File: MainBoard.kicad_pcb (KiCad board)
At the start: 4 copper layers, 102 parts, among them J1 USB B Mini, J5 Audio Out Port, P1 CARTRIDGE_SLOT, P2 FRONT_PANEL_CONNECTOR, P4 Multi AV Out, Q1 2SC4699, SW1 RESET, U1 S-CPU, U11 PST529D, U13 S-SMP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

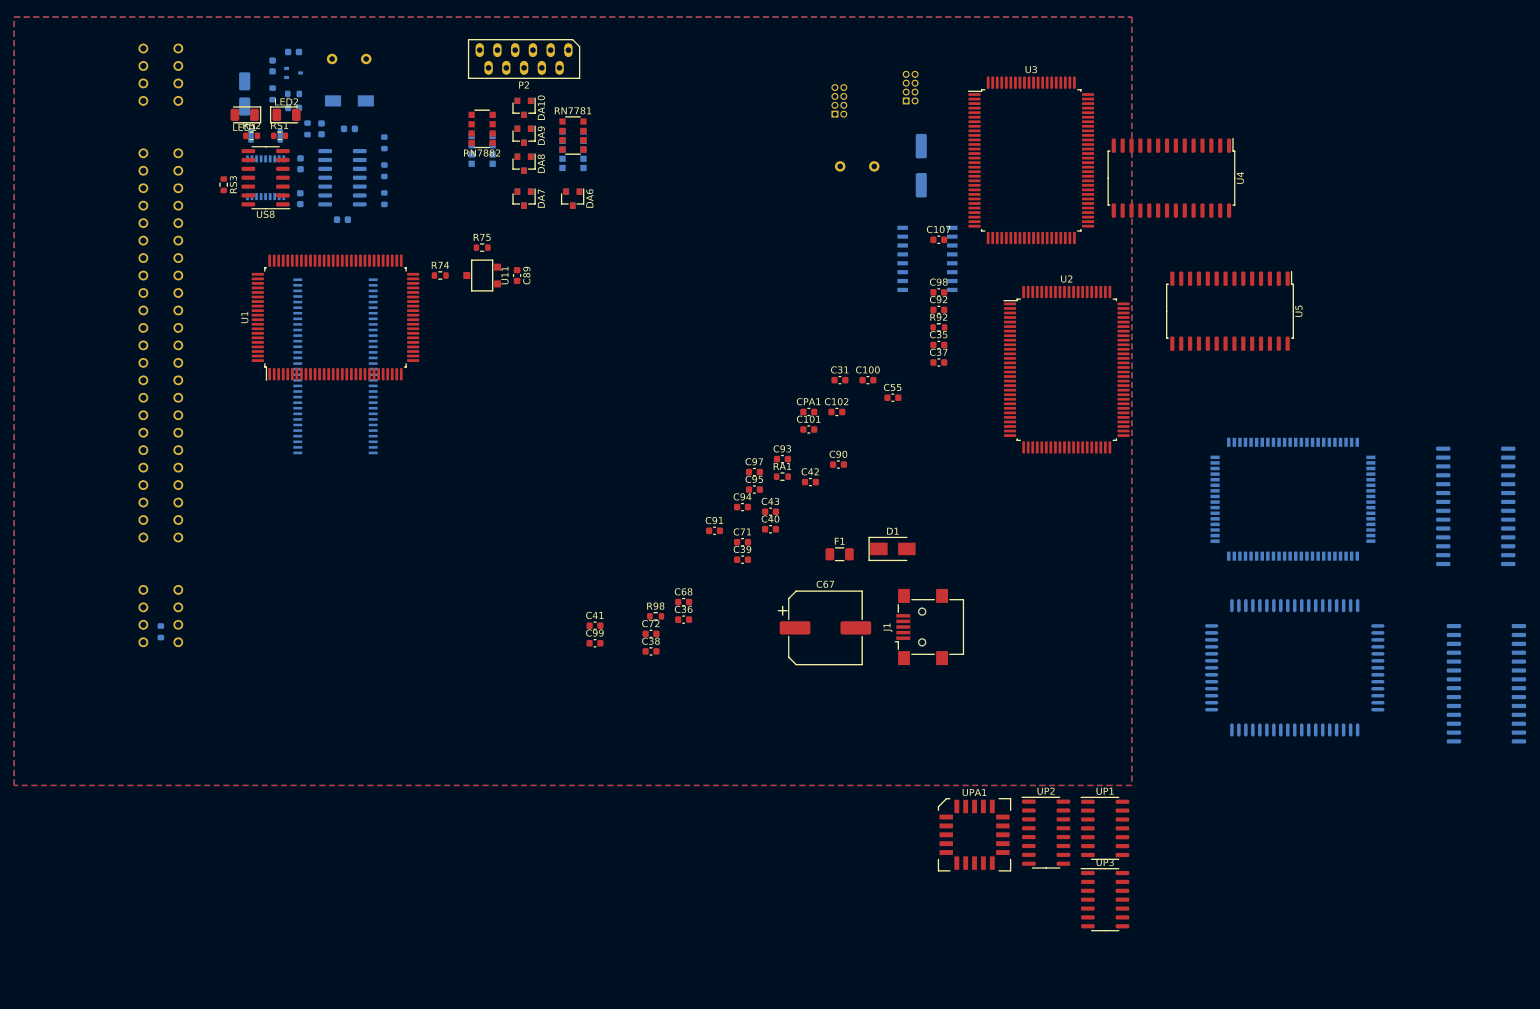
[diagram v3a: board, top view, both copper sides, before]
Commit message: Component layout is done
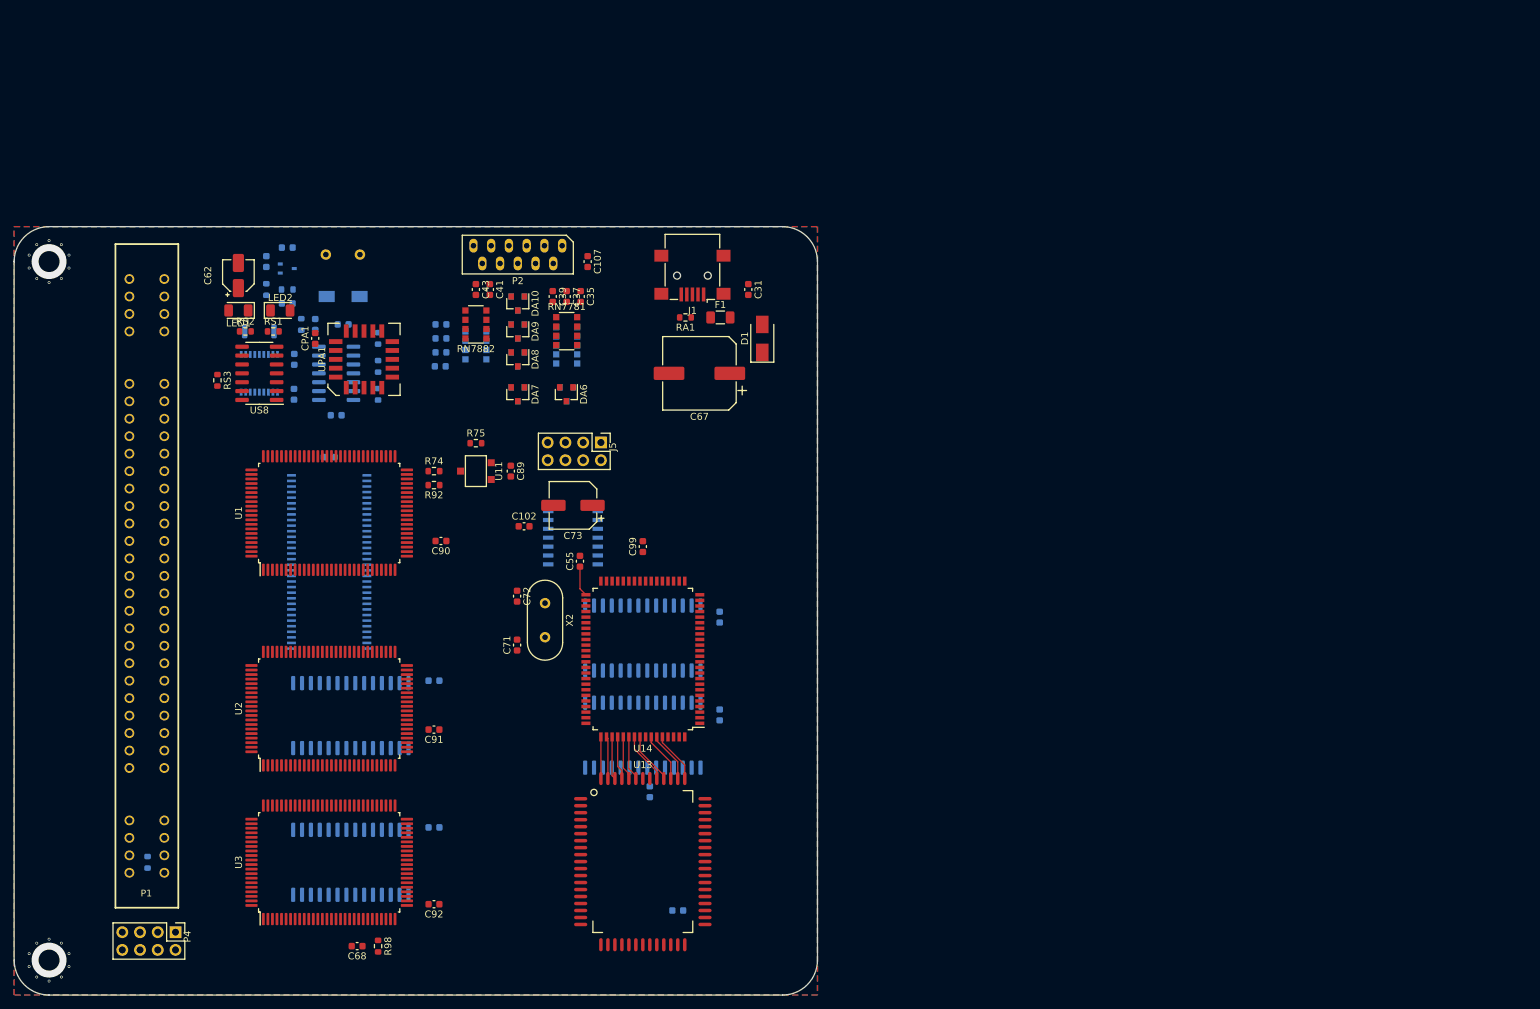
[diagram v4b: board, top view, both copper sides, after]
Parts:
- removed UP1, UP3: 74LS125, Package_SO:SOIC-14_3.9x8.7mm_P1.27mm
- removed UP2: 74LS133, Package_SO:SOIC-16_3.9x9.9mm_P1.27mm
- C100, C101, C36, C38, C40, C42, C93, C94, C95, C97, C98, U4, U5: moved to B.Cu
- C62, C73, P1, U13, U14, X2: moved to F.Cu
- J5, P4: footprint Connector_PinHeader_1.27mm:PinHeader_2x04_P1.27mm_Vertical -> Connector_PinHeader_2.54mm:PinHeader_2x04_P2.54mm_Vertical; moved to F.Cu
- moved P4 158.4 mm to (43.1, 151.0), turned to 270 degrees
- moved U4 153.0 mm to (68.2, 141.0), turned to 90 degrees
- moved U3 142.1 mm to (65.1, 141.0), turned to 90 degrees
- moved U5 138.5 mm to (68.2, 120.0), turned to 90 degrees
- moved U15 121.0 mm to (110.0, 122.8), turned to 90 degrees
- moved U16 120.7 mm to (110.0, 108.9), turned to 90 degrees
- moved U2 116.2 mm to (65.1, 119.0), turned to 90 degrees
- moved C92 111.6 mm to (80.1, 147.0), turned to 180 degrees
- moved UPA1 110.8 mm to (70.1, 69.0), turned to 90 degrees
- moved U13 97.4 mm to (110.0, 140.9), turned to 0 degrees
- moved U14 95.8 mm to (110.0, 111.9), turned to 180 degrees
- moved C98 82.6 mm to (111.0, 130.9), turned to 90 degrees
- moved R92 75.7 mm to (80.1, 87.0), turned to 180 degrees
- moved X2 75.5 mm to (96.0, 103.9), turned to 270 degrees
- moved C93 72.6 mm to (80.1, 136.0), turned to 180 degrees
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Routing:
- net Net-(U13-Pad55): track 0.00 -> 7.36 mm
- net Net-(U13-Pad56): track 0.00 -> 7.28 mm
- net Net-(U13-Pad52): track 0.00 -> 7.28 mm
- net Net-(U13-Pad53): track 0.00 -> 7.19 mm
- net Net-(U13-Pad54): track 0.00 -> 7.11 mm
- net Net-(U13-Pad59): track 0.00 -> 6.36 mm
- net Net-(U13-Pad60): track 0.00 -> 6.28 mm
- net Net-(U13-Pad61): track 0.00 -> 6.20 mm
- net Net-(U13-Pad62): track 0.00 -> 6.12 mm
- net Net-(U13-Pad63): track 0.00 -> 6.03 mm
- net Net-(U13-Pad64): track 0.00 -> 5.95 mm
- net /SCLK: track 0.00 -> 4.38 mm
- net VCC: vias 0 -> 20
- net GND: vias 0 -> 2
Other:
- board outline added: 115 x 110 mm
- net class Default: clearance 0.127 -> 0.16; trace_width 0.127 -> 0.16
- net class Power: clearance 0.127 -> 0.16; trace_width 0.508 -> 0.32; via_dia 0.508 -> 0.5
- rule trace_clearance: 0.127 -> 0.16
- rule trace_min: 0.08 -> 0.16

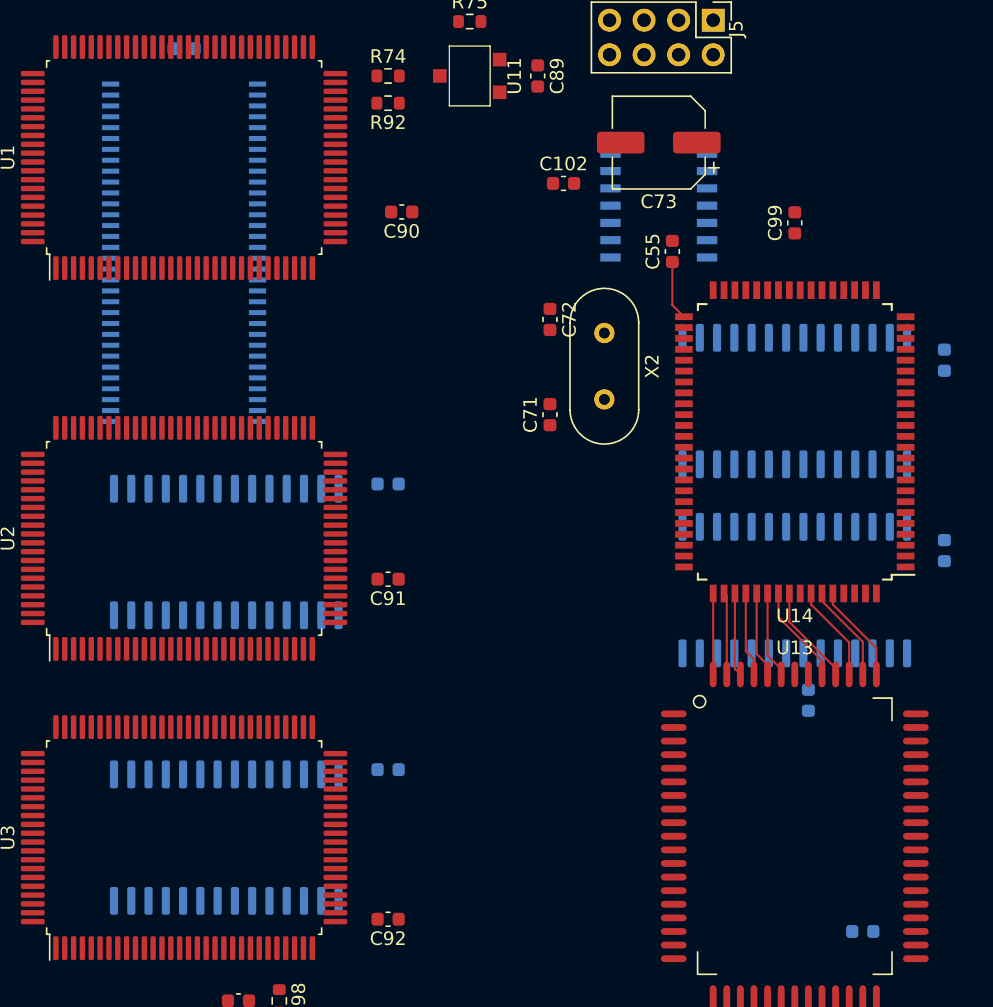
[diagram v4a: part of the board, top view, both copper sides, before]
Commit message: Fixed wrong SRAM/PSRAM footprints
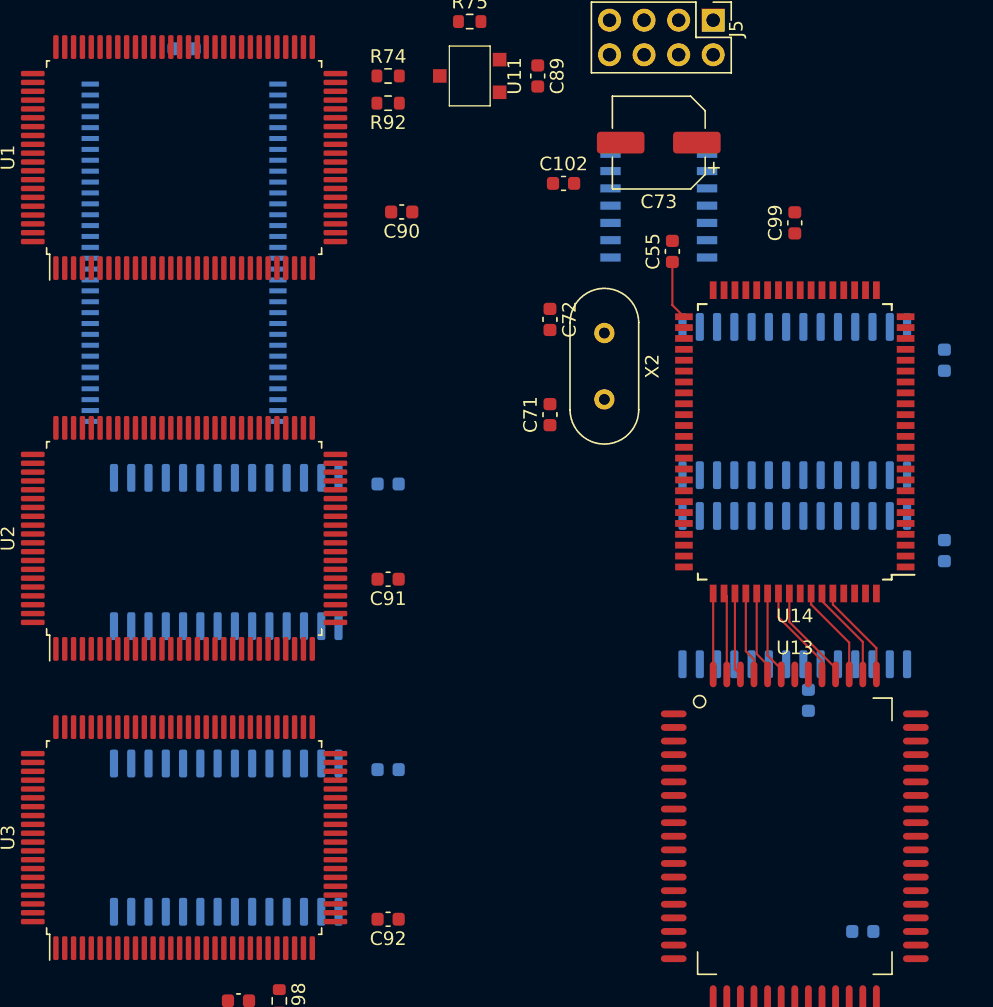
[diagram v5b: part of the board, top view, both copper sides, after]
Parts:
- U15, U16, U4, U5: footprint SNES:SOIC-28W_7.5x17.9mm_P1.27mm -> SNES:SOP-28-330mil_P1.27mm

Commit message: Footprints reassigned, playing around PSRAM
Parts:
- U17: footprint SNES:SOIC-16W_5.3x10.2mm_P1.27mm -> SNES:SOP-16-300mil_P1.27mm
- moved C98 3.26 mm to (110.0, 134.0)
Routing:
- net VCC: track 0.00 -> 14.7 mm, vias 20 -> 21
- net /MA5: track 0.00 -> 14.5 mm
- net /MA2: track 0.00 -> 14.3 mm
- net /~OE: track 0.00 -> 14.3 mm
- net /MA4: track 0.00 -> 14.3 mm
- net /MA3: track 0.00 -> 14.3 mm
- net /MA1: track 0.00 -> 14.3 mm
- net /MA9: track 0.00 -> 14.3 mm
- net /MA11: track 0.00 -> 14.3 mm
- net /MA10: track 0.00 -> 14.3 mm

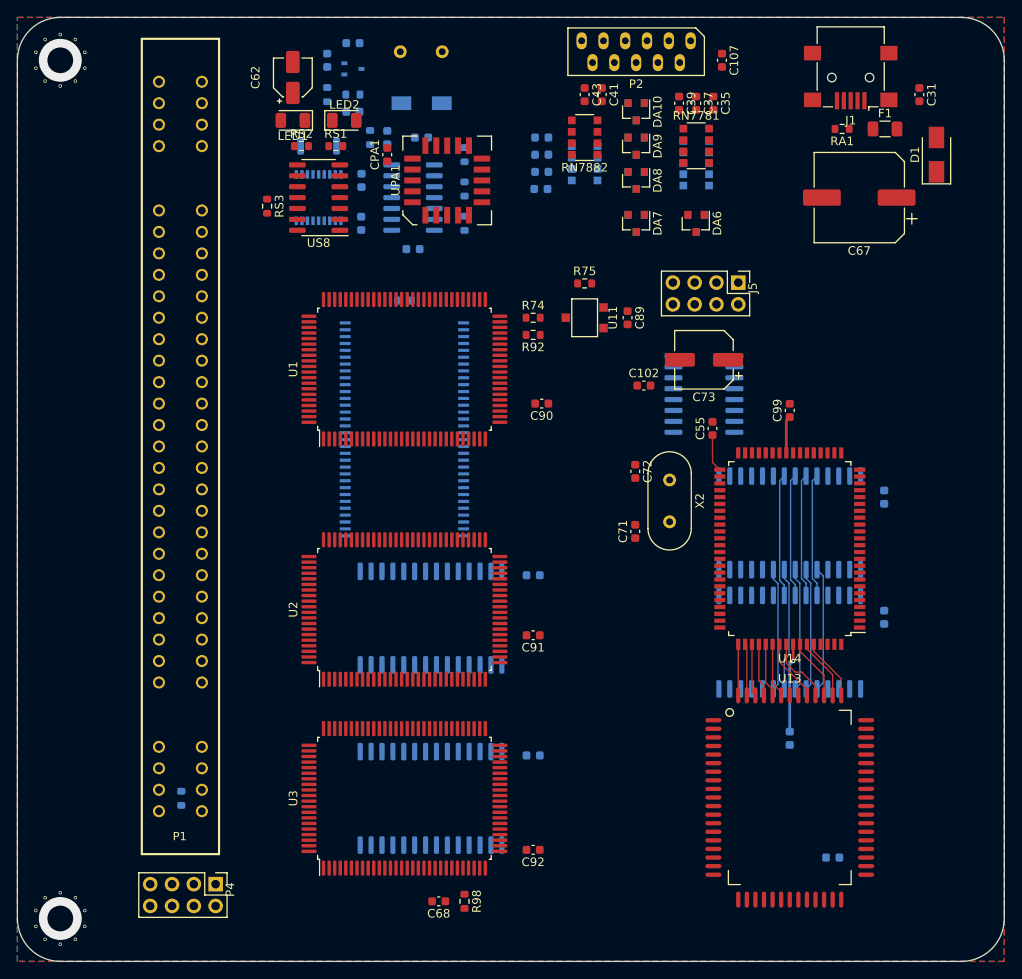
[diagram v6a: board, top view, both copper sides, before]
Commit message: Resized, refilled DC in section, compacted
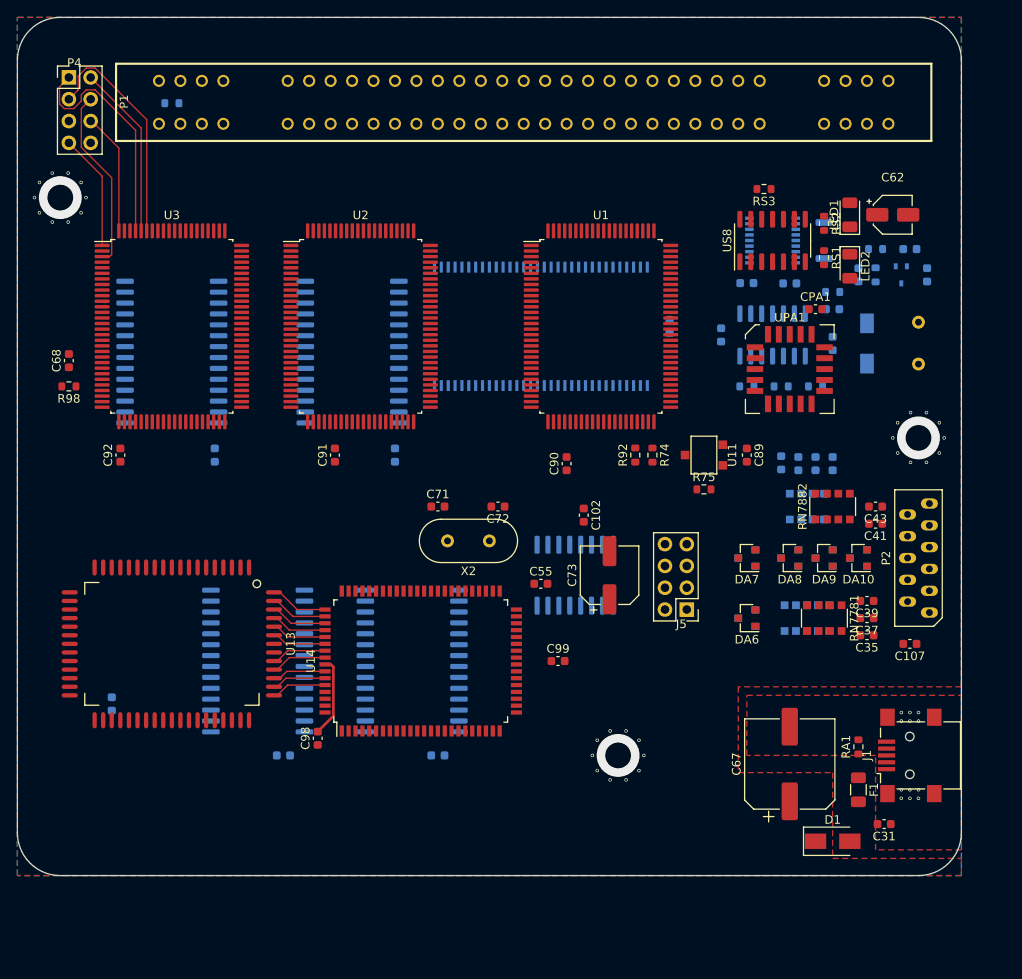
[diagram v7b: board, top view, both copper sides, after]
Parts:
- C98: moved to F.Cu
- moved P4 95.5 mm to (26.0, 57.0), turned to 0 degrees
- moved C97 85.9 mm to (31.0, 130.0), turned to 90 degrees
- moved C31 85.1 mm to (121.0, 144.0), turned to 180 degrees
- moved R97 81.0 mm to (38.0, 60.0), turned to 0 degrees
- moved D1 80.9 mm to (115.0, 146.0), turned to 0 degrees
- moved J1 79.3 mm to (124.0, 136.0), turned to 90 degrees
- moved F1 77.1 mm to (118.0, 140.0), turned to 270 degrees
- moved C68 76.3 mm to (26.0, 90.0), turned to 90 degrees
- moved R98 75.7 mm to (26.0, 93.0), turned to 180 degrees
- moved U13 74.2 mm to (38.0, 123.0), turned to 270 degrees
- moved C1 72.1 mm to (126.0, 80.0), turned to 90 degrees
- moved RA1 72.0 mm to (118.0, 135.0), turned to 90 degrees
- moved C101 71.8 mm to (51.0, 136.0), turned to 0 degrees
- moved C62 71.7 mm to (122.0, 73.0), turned to 0 degrees
- moved C107 71.4 mm to (124.0, 123.0), turned to 180 degrees
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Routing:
- net /VIDEO_R: track 0.00 -> 27.6 mm
- net /VIDEO_B: track 0.00 -> 27.0 mm
- net /3.58M: track 0.00 -> 21.2 mm
- net /VIDEO_G: track 0.00 -> 20.3 mm
- net /MA5: track 14.5 -> 0.00 mm
- net /MA2: track 14.3 -> 0.00 mm
- net /~OE: track 14.3 -> 0.00 mm
- net /MA4: track 14.3 -> 0.00 mm
- net /MA3: track 14.3 -> 0.00 mm
- net /MA1: track 14.3 -> 0.00 mm
- net /MA9: track 14.3 -> 0.00 mm
- net /MA11: track 14.3 -> 0.00 mm
- net /MA10: track 14.3 -> 0.00 mm
- net /~VIDEO_BURST: track 0.00 -> 14.2 mm
- net /~VIDEO_CSYNC: track 0.00 -> 13.6 mm
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- added copper zone on F.Cu, net GND
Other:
- board size 115 x 110 mm -> 110 x 100 mm
